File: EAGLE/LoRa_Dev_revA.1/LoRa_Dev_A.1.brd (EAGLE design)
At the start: 38.1 x 25.4 mm, 28 parts, among them IC1 HMC8038LP4CETR, IC2 SX1262IMLTRT, J1 U.FL-R-SMT-1_80_, J2 HEADER_12PIN

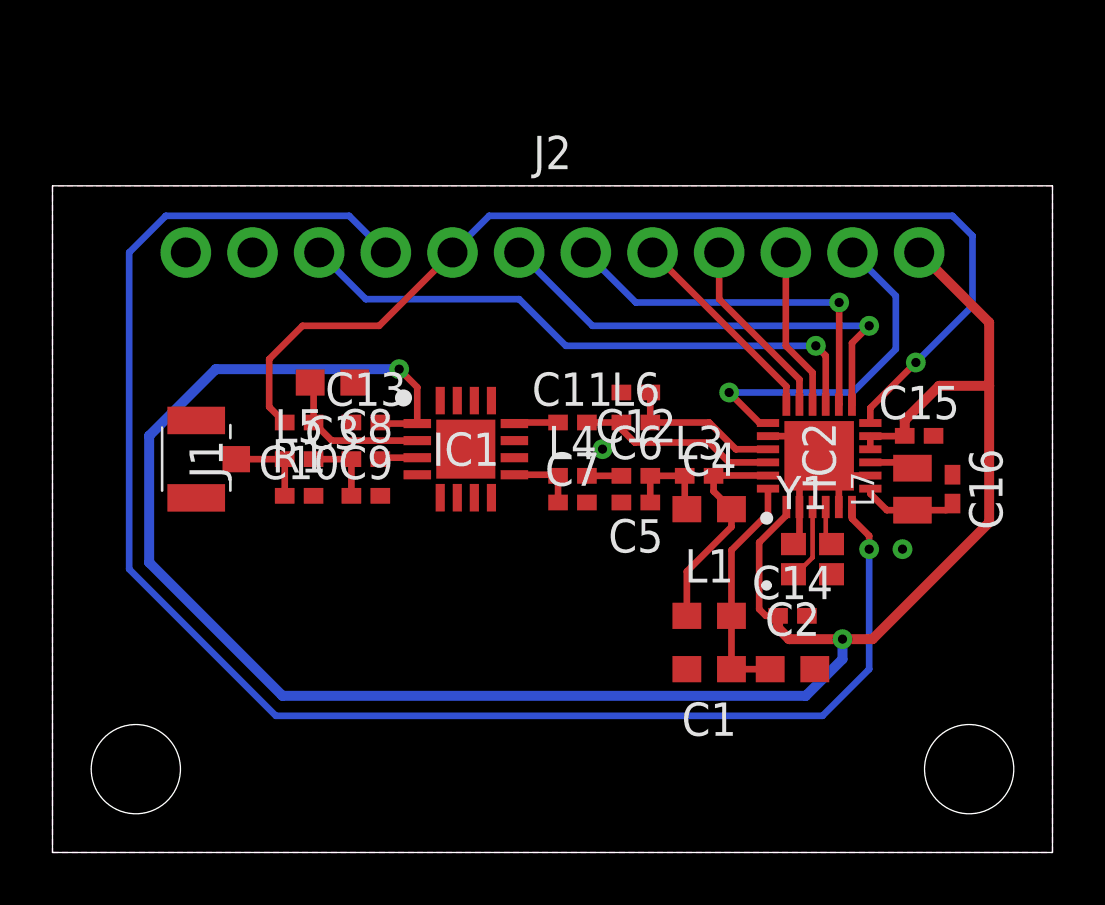
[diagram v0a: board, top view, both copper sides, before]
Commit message: LoRa Silkscreen
Silkscreen and gerber files added
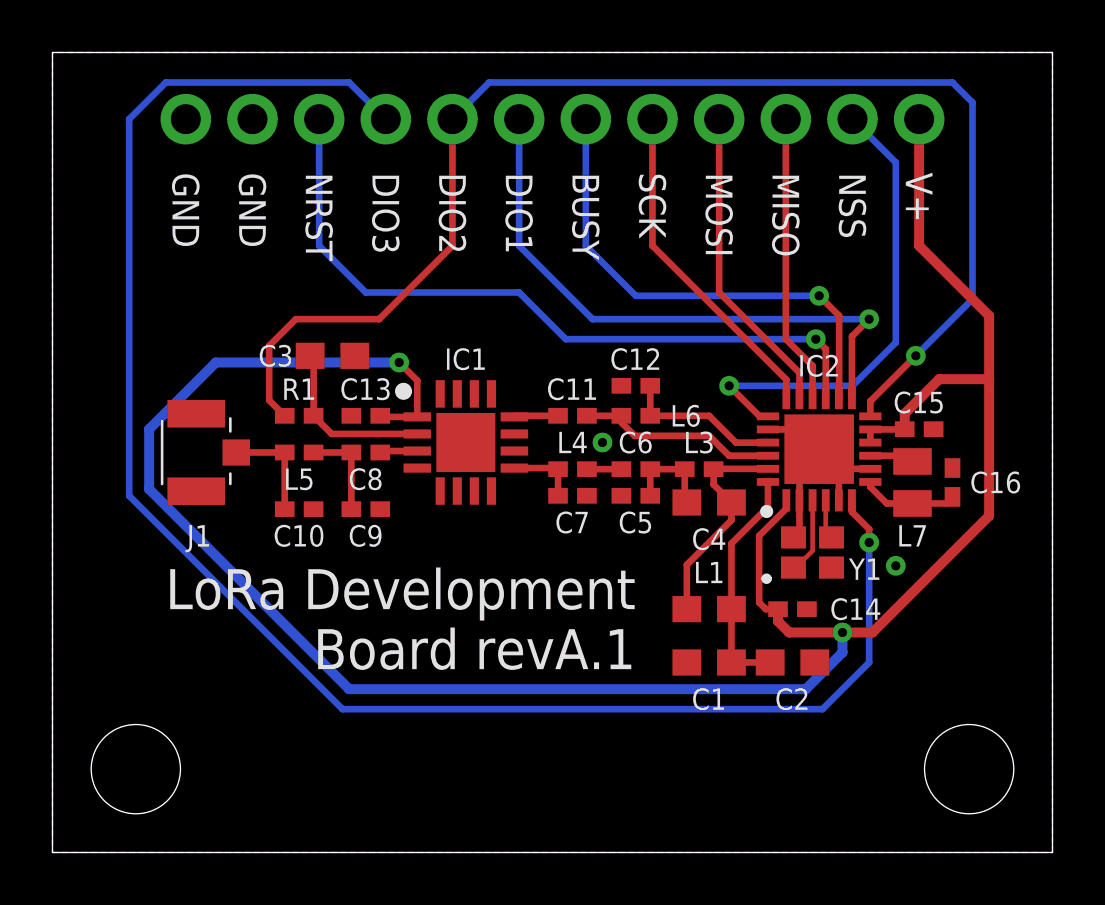
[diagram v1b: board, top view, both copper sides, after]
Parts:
- L1: value (none) -> 47nH
- Y1: value (none) -> 32MHz
- moved J2 5.08 mm to (19.1, 27.9)
- moved C3 1.02 mm to (10.7, 18.9)
- moved C10 0.51 mm to (9.40, 13.1)
- moved C9 0.51 mm to (11.9, 13.1)
- moved C11 0.25 mm to (19.8, 16.6)
- moved C12 0.25 mm to (22.2, 17.8)
- moved C13 0.25 mm to (11.9, 16.6)
- moved C14 0.25 mm to (28.2, 9.27)
- moved C15 0.25 mm to (33.0, 16.1)
- moved C4 0.25 mm to (25.0, 13.3)
- moved IC2 0.25 mm to (29.2, 15.4)
- moved L1 0.25 mm to (25.0, 9.27)
- moved L6 0.25 mm to (22.2, 16.6)
- moved R1 0.25 mm to (9.40, 16.6)
- moved C1 0.25 mm to (25.0, 7.24)
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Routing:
- net DIO2: track 40.8 -> 50.6 mm
- net NSS: track 13.4 -> 18.2 mm
- net SCK: track 7.91 -> 12.7 mm
- net NRESET: track 22.8 -> 27.6 mm
- net MOSI: track 7.06 -> 11.9 mm
- net MISO: track 6.22 -> 11.0 mm
- net DIO1: track 17.8 -> 22.6 mm
- net BUSY: track 14.3 -> 18.7 mm
- net +3V3: track 82.3 -> 85.6 mm
- net DIO3: track 60.7 -> 64.0 mm
- net GND: track 10.6 -> 9.53 mm
- net N$2: track 3.09 -> 3.85 mm
- net N$1: track 3.24 -> 4.01 mm
- net N$4: track 5.81 -> 6.58 mm
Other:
- board size 38.1 x 25.4 mm -> 38.1 x 30.5 mm
- board text added: "BUSY"
- board text added: "DIO1"
- board text added: "DIO2"
- board text added: "DIO3"
- board text added: "GND"
- board text added: "LoRa Development Board revA.1"
- board text added: "MISO"
- board text added: "MOSI"
- board text added: "NRST"
- board text added: "NSE LABS"
- board text added: "NSS"
- board text added: "SCK"
- board text added: "V+"

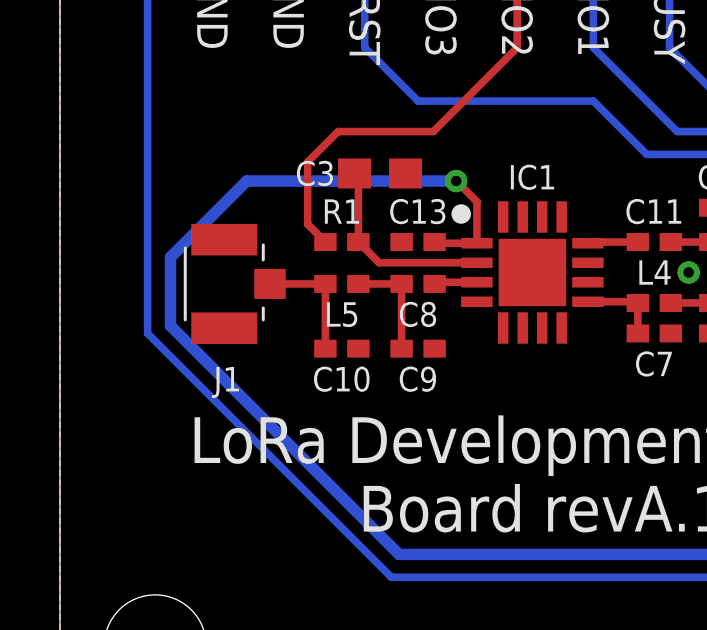
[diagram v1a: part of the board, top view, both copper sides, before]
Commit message: Gerber and Fab Files created
silkscreen and origin modified
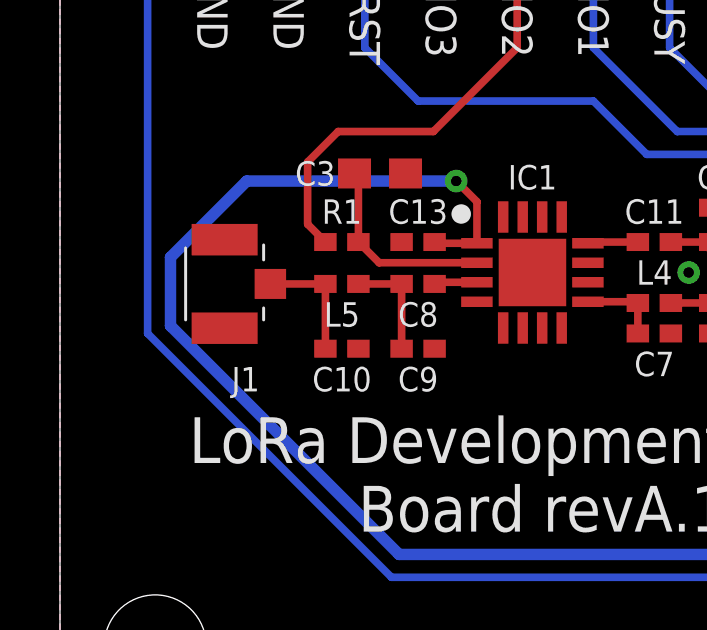
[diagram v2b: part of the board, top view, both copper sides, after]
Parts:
- moved J1 0.60 mm to (6.19, 15.2)
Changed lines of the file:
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@@
 <setting verticaltext="up"/>
 </settings>
-<grid distance="0.25" unitdist="inch" unit="inch" style="lines" multiple="1" display="no" altdistance="5" altunitdist="mil" altunit="mil"/>
+<grid distance="1.2" unitdist="mm" unit="mm" style="lines" multiple="1" display="no" altdistance="5" altunitdist="mil" altunit="mil"/>
 <layers>
 <layer number="1" name="Top" color="4" fill="1" visible="yes" active="yes"/>
@@
 <attribute name="VALUE" x="11.938" y="15.367" size="1.27" layer="27" align="center"/>
 </element>
-<element name="J1" library="NSE LABS" package="UFLRSMT180" value="U.FL-R-SMT-1_80_" x="5.588" y="15.24" smashed="yes" rot="R90">
-<attribute name="ARROW_PART_NUMBER" value="" x="5.588" y="15.24" size="1.016" layer="27" font="vector" rot="R90" display="off"/>
-<attribute name="ARROW_PRICE-STOCK" value="" x="5.588" y="15.24" size="1.016" layer="27" font="vector" rot="R90" display="off"/>
-<attribute name="DESCRIPTION" value="RF Connectors/Coaxial Connectors SMD RoHS" x="5.588" y="15.24" size="1.016" layer="27" font="vector" rot="R90" display="off"/>
-<attribute name="HEIGHT" value="1.45mm" x="5.588" y="15.24" size="1.016" layer="27" font="vector" rot="R90" display="off"/>
-<attribute name="MANUFACTURER_NAME" value="Hirose" x="5.588" y="15.24" size="1.016" layer="27" font="vector" rot="R90" display="off"/>
-<attribute name="MANUFACTURER_PART_NUMBER" value="U.FL-R-SMT-1(80)" x="5.588" y="15.24" size="1.016" layer="27" font="vector" rot="R90" display="off"/>
-<attribute name="MOUSER_PART_NUMBER" value="798-UFLRSMT180" x="5.588" y="15.24" size="1.016" layer="27" font="vector" rot="R90" display="off"/>
-<attribute name="MOUSER_PRICE-STOCK" value="https://www.mouser.co.uk/ProductDetail/Hirose-Connector/U.FL-R-SMT-180?qs=PABxe4V6HDqFClp15N8Kig%3D%3D" x="5.588" y="15.24" size="1.016" layer="27" font="vector" rot="R90" display="off"/>
-<attribute name="NAME" x="5.588" y="12.065" size="0.8128" layer="25" font="vector" rot="R180" align="center"/>
-<attribute name="VALUE" x="5.851" y="15.24" size="1.27" layer="27" rot="R90" align="center"/>
+<element name="J1" library="NSE LABS" package="UFLRSMT180" value="U.FL-R-SMT-1_80_" x="6.188" y="15.24" smashed="yes" rot="R90">
+<attribute name="ARROW_PART_NUMBER" value="" x="6.188" y="15.24" size="1.016" layer="27" font="vector" rot="R90" display="off"/>
+<attribute name="ARROW_PRICE-STOCK" value="" x="6.188" y="15.24" size="1.016" layer="27" font="vector" rot="R90" display="off"/>
+<attribute name="DESCRIPTION" value="RF Connectors/Coaxial Connectors SMD RoHS" x="6.188" y="15.24" size="1.016" layer="27" font="vector" rot="R90" display="off"/>
+<attribute name="HEIGHT" value="1.45mm" x="6.188" y="15.24" size="1.016" layer="27" font="vector" rot="R90" display="off"/>
+<attribute name="MANUFACTURER_NAME" value="Hirose" x="6.188" y="15.24" size="1.016" layer="27" font="vector" rot="R90" display="off"/>
+<attribute name="MANUFACTURER_PART_NUMBER" value="U.FL-R-SMT-1(80)" x="6.188" y="15.24" size="1.016" layer="27" font="vector" rot="R90" display="off"/>
+<attribute name="MOUSER_PART_NUMBER" value="798-UFLRSMT180" x="6.188" y="15.24" size="1.016" layer="27" font="vector" rot="R90" display="off"/>
+<attribute name="MOUSER_PRICE-STOCK" value="https://www.mouser.co.uk/ProductDetail/Hirose-Connector/U.FL-R-SMT-180?qs=PABxe4V6HDqFClp15N8Kig%3D%3D" x="6.188" y="15.24" size="1.016" layer="27" font="vector" rot="R90" display="off"/>
+<attribute name="NAME" x="6.188" y="12.065" size="0.8128" layer="25" font="vector" rot="R180" align="center"/>
+<attribute name="VALUE" x="6.451" y="15.24" size="1.27" layer="27" rot="R90" align="center"/>
 </element>
 <element name="IC2" library="NSE LABS" package="QFN50P400X400X100-25N" value="SX1262IMLTRT" x="29.21" y="15.367" smashed="yes" rot="R90">
@@
 <contactref element="J1" pad="1"/>
 <wire x1="8.848" y1="13.081" x2="8.848" y2="15.24" width="0.254" layer="1"/>
-<wire x1="8.848" y1="15.24" x2="7.001" y2="15.24" width="0.254" layer="1"/>
+<wire x1="8.848" y1="15.24" x2="7.013" y2="15.24" width="0.254" layer="1"/>
 </signal>
 <signal name="N$2">
@@
 </signals>
 <mfgpreviewcolors>
-<mfgpreviewcolor name="soldermaskcolor" color="0xC8008000"/>
+<mfgpreviewcolor name="soldermaskcolor" color="0xC800AA00"/>
 <mfgpreviewcolor name="silkscreencolor" color="0xFFFEFEFE"/>
-<mfgpreviewcolor name="backgroundcolor" color="0xFF282828"/>
+<mfgpreviewcolor name="backgroundcolor" color="0xFF000000"/>
 <mfgpreviewcolor name="coppercolor" color="0xFFFFBF00"/>
 <mfgpreviewcolor name="substratecolor" color="0xFF786E46"/>
